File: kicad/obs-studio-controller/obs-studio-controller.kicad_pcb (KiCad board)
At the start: 2 copper layers, 70 parts, among them J1 PWR_SWITCH, J2 EXT_PWR, J3 LEDS, J4 Conn_Display, J5 Conn_02x08_Odd_Even, Q1 2N7002, Q2 SS8050_C2150, Q3 SS8050_C2150, SW1 RotaryEncoder_Switch, SW2 RotaryEncoder_Switch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

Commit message: Routing complete
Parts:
- removed D1: LED5V, LED_SMD:LED_0603_1608Metric
- removed R3: 1k, Resistor_SMD:R_0402_1005Metric
- added J6: GPIO, Connector_PinSocket_2.54mm:PinSocket_1x06_P2.54mm_Vertical, F.Cu at (80.0, 44.0)
- added J7: WS2812, Connector_PinSocket_2.54mm:PinSocket_1x03_P2.54mm_Vertical, F.Cu at (97.5, 19.4)
- J4: footprint Connector_PinHeader_2.54mm:PinHeader_1x08_P2.54mm_Vertical -> custom:DISPLAY
- J5: value Conn_02x08_Odd_Even -> BUTTONS
- moved C9 185.6 mm to (15.5, 19.5), turned to 90 degrees
- moved U5 182.9 mm to (36.5, -26.1), turned to 90 degrees
- moved C10 178.3 mm to (16.9, 19.5), turned to -90 degrees
- moved R12 172.4 mm to (0.00, -17.0), turned to -90 degrees
- moved R19 172.2 mm to (60.0, -17.0), turned to -90 degrees
- moved R10 166.5 mm to (0.00, 3.15), turned to 90 degrees
- moved R11 154.6 mm to (5.00, 3.15), turned to -90 degrees
- moved SW1 154.6 mm to (0.00, 0.00), turned to 90 degrees
- moved R13 151.4 mm to (13.0, 34.8), turned to 180 degrees
- moved R18 150.0 mm to (65.0, 3.15), turned to -90 degrees
- moved R17 148.5 mm to (60.0, 3.15), turned to 90 degrees
- moved Q1 145.9 mm to (16.5, 35.7)
- moved SW3 145.2 mm to (60.0, 0.00), turned to 90 degrees
- moved R20 142.7 mm to (90.0, 3.15), turned to 90 degrees
- moved R22 139.0 mm to (90.0, -17.0), turned to -90 degrees
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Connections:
- C10 pad 2: /Flasher/3V3 -> +3V3
- C3 pad 2: /Flasher/5V -> /AMS1117-5V-3v3/5V
- C4 pad 2: /Flasher/3V3 -> +3V3
- C7 pad 2: /Flasher/5V -> /AMS1117-5V-3v3/5V
- C8 pad 2: /Flasher/5V -> /AMS1117-5V-3v3/5V
- C9 pad 1: /Flasher/3V3 -> +3V3
- J1 pad 1: /+5V -> /AMS1117-5V-3v3/5V
- J1 pad 2: /Flasher/5V -> /VEXT
- J2 pad 3: /Flasher/5V -> /VEXT
- J4 pad 2: +3.3V -> +3V3
- J4 pad 5: +3.3V -> +3V3
- J5 pad 10: /BTN_IN2 -> /BTN_IN3
- J5 pad 12: /BTN_IN2 -> /BTN_IN3
- J5 pad 14: /BTN_IN2 -> /BTN_IN4
- J5 pad 16: /BTN_IN2 -> /BTN_IN4
- J5 pad 6: /BTN_IN1 -> /BTN_IN2
- J5 pad 8: /BTN_IN1 -> /BTN_IN2
- JP1 pad 1: /Flasher/5V -> /VEXT
- JP1 pad 2: /+5V -> /AMS1117-5V-3v3/5V
- R27 pad 2: /Flasher/3V3 -> +3V3
- R28 pad 2: /Flasher/3V3 -> +3V3
- R29 pad 1: /Flasher/3V3 -> +3V3
- R30 pad 1: /Flasher/3V3 -> +3V3
- R31 pad 1: /Flasher/3V3 -> +3V3
- R32 pad 1: /Flasher/5V -> /AMS1117-5V-3v3/5V
- U1 pad 11: unconnected-(U1-Pad11) -> /IO26
- U1 pad 12: unconnected-(U1-Pad12) -> /IO27
- U1 pad 27: unconnected-(U1-Pad27) -> /BTN_IN3
- U1 pad 28: unconnected-(U1-Pad28) -> /BTN_IN4
- U1 pad 29: unconnected-(U1-Pad29) -> /IO5
- U1 pad 6: unconnected-(U1-Pad6) -> /IO34
- U1 pad 7: unconnected-(U1-Pad7) -> /EXT_SENSE
- U1 pad 8: unconnected-(U1-Pad8) -> /IO32
- U1 pad 9: unconnected-(U1-Pad9) -> /IO33
- U4 pad 15: /Flasher/3V3 -> +3V3
- U4 pad 16: /Flasher/5V -> /AMS1117-5V-3v3/5V
- U4 pad 7: /Flasher/5V -> /AMS1117-5V-3v3/5V
- U5 pad 2: /Flasher/3V3 -> +3V3
- U5 pad 3: /Flasher/5V -> /AMS1117-5V-3v3/5V
- USBC1 pad A4-B9: /Flasher/5V -> /AMS1117-5V-3v3/5V
- USBC1 pad B4-A9: /Flasher/5V -> /AMS1117-5V-3v3/5V
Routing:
- net +3V3: track 0.00 -> 291.8 mm, vias 0 -> 27
- net /AMS1117-5V-3v3/5V: track 0.00 -> 153.5 mm, vias 0 -> 1
- net /Flasher/ESP_TX: track 0.00 -> 124.3 mm, vias 0 -> 4
- net /BUTTON_4: track 0.00 -> 122.1 mm, vias 0 -> 1
- net /Flasher/ESP_RX: track 0.00 -> 120.6 mm, vias 0 -> 2
- net /IO5: track 0.00 -> 104.6 mm, vias 0 -> 2
- net /EXT_MONITOR: track 0.00 -> 101.2 mm, vias 0 -> 4
- net /Flasher/ESP_EN: track 0.00 -> 91.4 mm, vias 0 -> 2
- net Net-(J3-Pad1): track 0.00 -> 90.1 mm
- net /Flasher/ESP_IO0: track 0.00 -> 85.0 mm, vias 0 -> 4
- net /BUTTON_3: track 0.00 -> 83.9 mm
- net Net-(J3-Pad3): track 0.00 -> 83.3 mm, vias 0 -> 2
- net /BTN_OUT: track 0.00 -> 79.4 mm, vias 0 -> 5
- net Net-(J3-Pad5): track 0.00 -> 78.2 mm, vias 0 -> 2
- net /BUTTON_2: track 0.00 -> 58.9 mm
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- added copper zone on B.Cu, net +3V3
- added copper zone on B.Cu, net GND
- added copper zone on F.Cu, net GND
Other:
- board outline added: 111 x 113.8 mm
- board text added: "+5V"
- board text added: "3V3"
- board text added: "IO16 IO17 IO34 IO33 IO32 IO27 IO26 IO5"
- board text added: "LEDS"
- board text added: "RX"
- board text added: "TX"
- board text added: "WS2812"

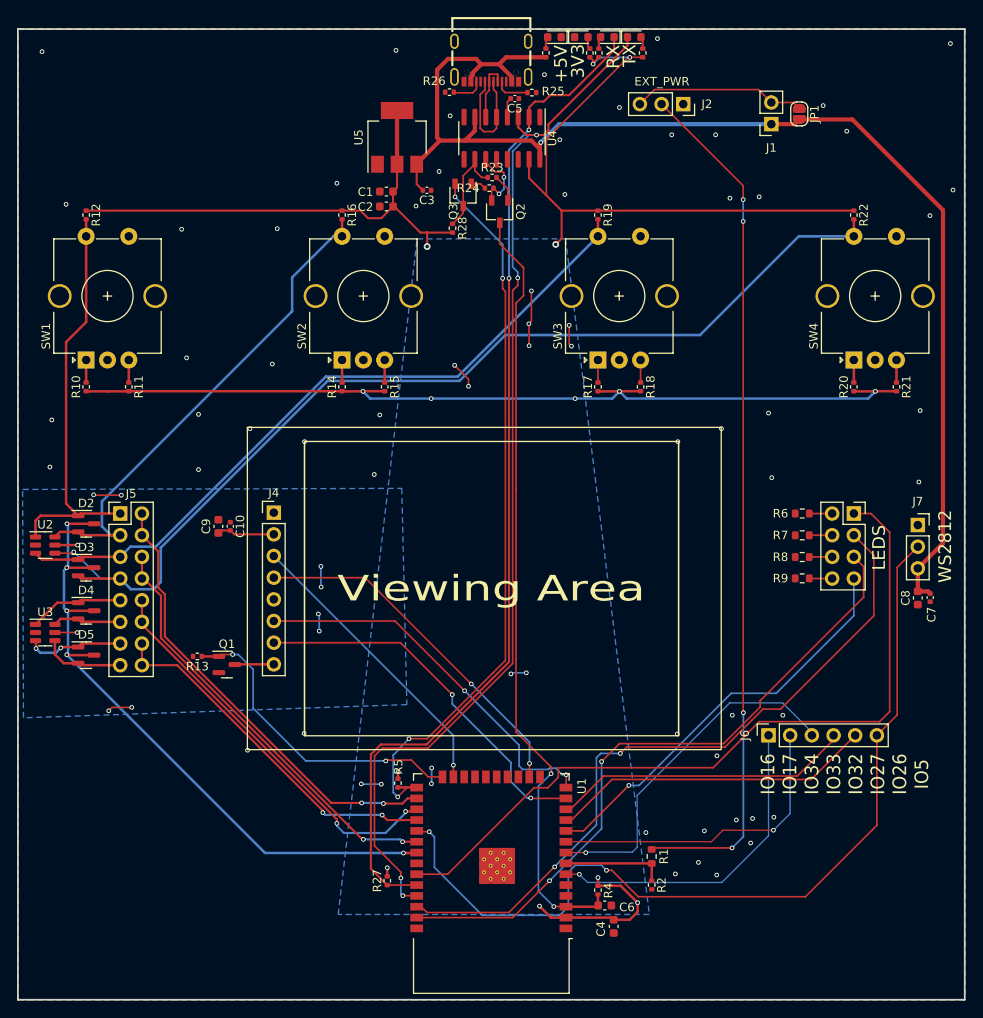
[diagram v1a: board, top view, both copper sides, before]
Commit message: Fixed label, changed edge cuts, added screw holes
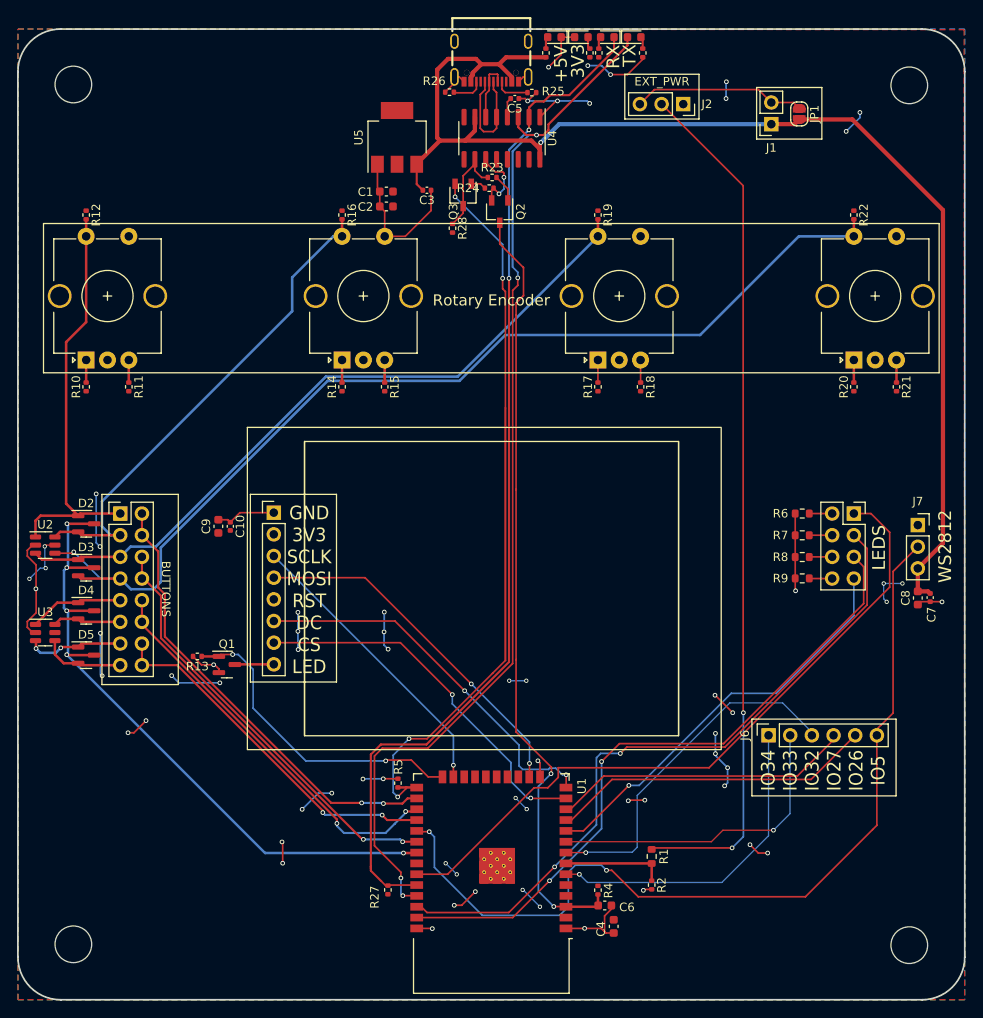
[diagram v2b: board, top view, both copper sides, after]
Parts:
- added REF**: MountingHole_4.3mm_M4, MountingHole:MountingHole_4.3mm_M4, F.Cu at (-1.50, 68.5)
- added REF**: MountingHole_4.3mm_M4, MountingHole:MountingHole_4.3mm_M4, F.Cu at (-1.50, -32.3)
- added REF**: MountingHole_4.3mm_M4, MountingHole:MountingHole_4.3mm_M4, F.Cu at (96.5, 68.6)
- added REF**: MountingHole_4.3mm_M4, MountingHole:MountingHole_4.3mm_M4, F.Cu at (96.5, -32.2)
- moved R27 1.08 mm to (35.4, 62.1), turned to -90 degrees
- renumbered SW4 to SWe
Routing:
- net +3V3: track 291.8 -> 74.3 mm, vias 27 -> 40
- net GND: track 10.5 -> 106.9 mm, vias 64 -> 24
- net Net-(J3-Pad1): track 90.1 -> 81.6 mm
- net Net-(J3-Pad3): track 83.3 -> 81.5 mm
- net /Flasher/ESP_RX: track 120.6 -> 121.2 mm
- net /EXT_MONITOR: vias 4 -> 2
- added copper zone on F.Cu, net +3V3
- removed copper zone on B.Cu, net +3V3
- removed copper zone on F.Cu, net GND
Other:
- outline, holes or cut-outs redrawn
- board text added: "BUTTONS"
- board text added: "GND 3V3 SCLK MOSI RST DC CS LED"
- board text added: "GND OUT +5V"
- board text added: "IO34 IO33 IO32 IO27 IO26 IO5"
- board text added: "Rotary Encoder"
- board text removed: "IO16 IO17 IO34 IO33 IO32 IO27 IO26 IO5"

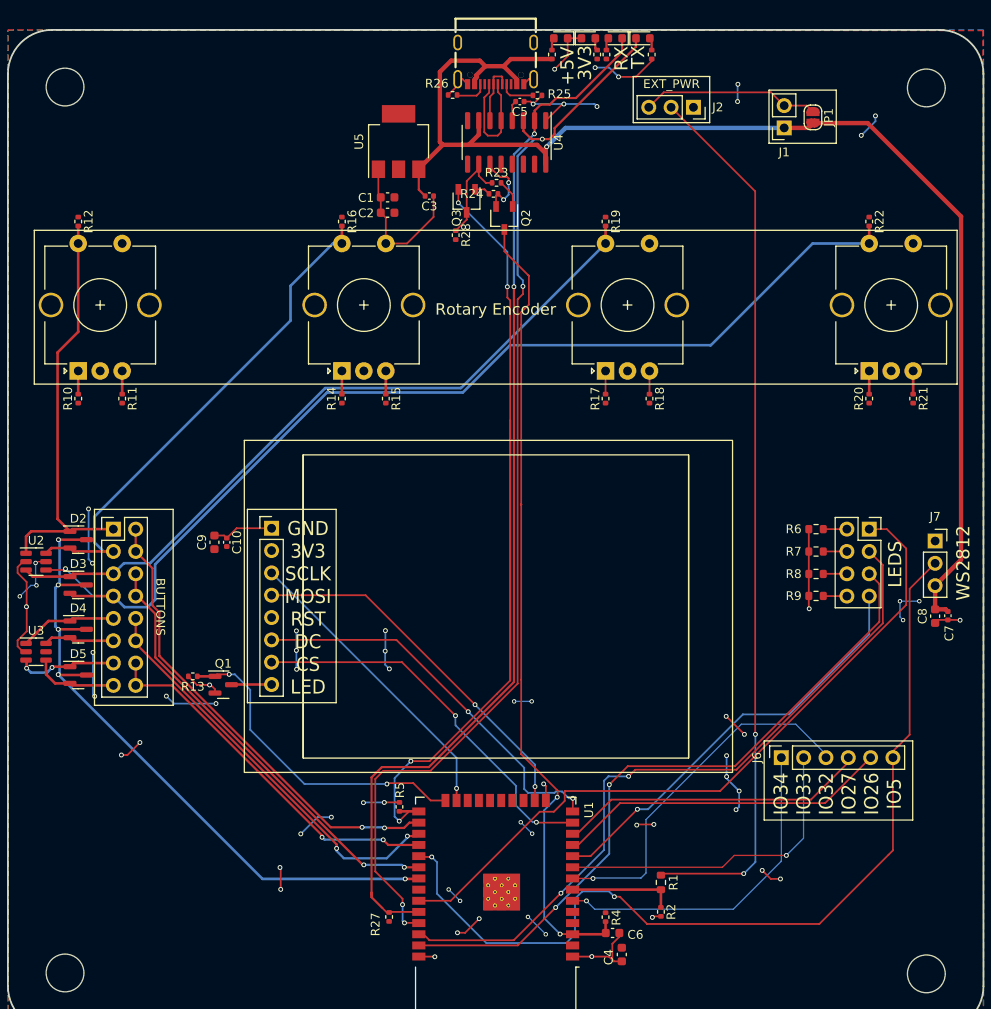
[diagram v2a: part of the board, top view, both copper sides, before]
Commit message: Added some labels
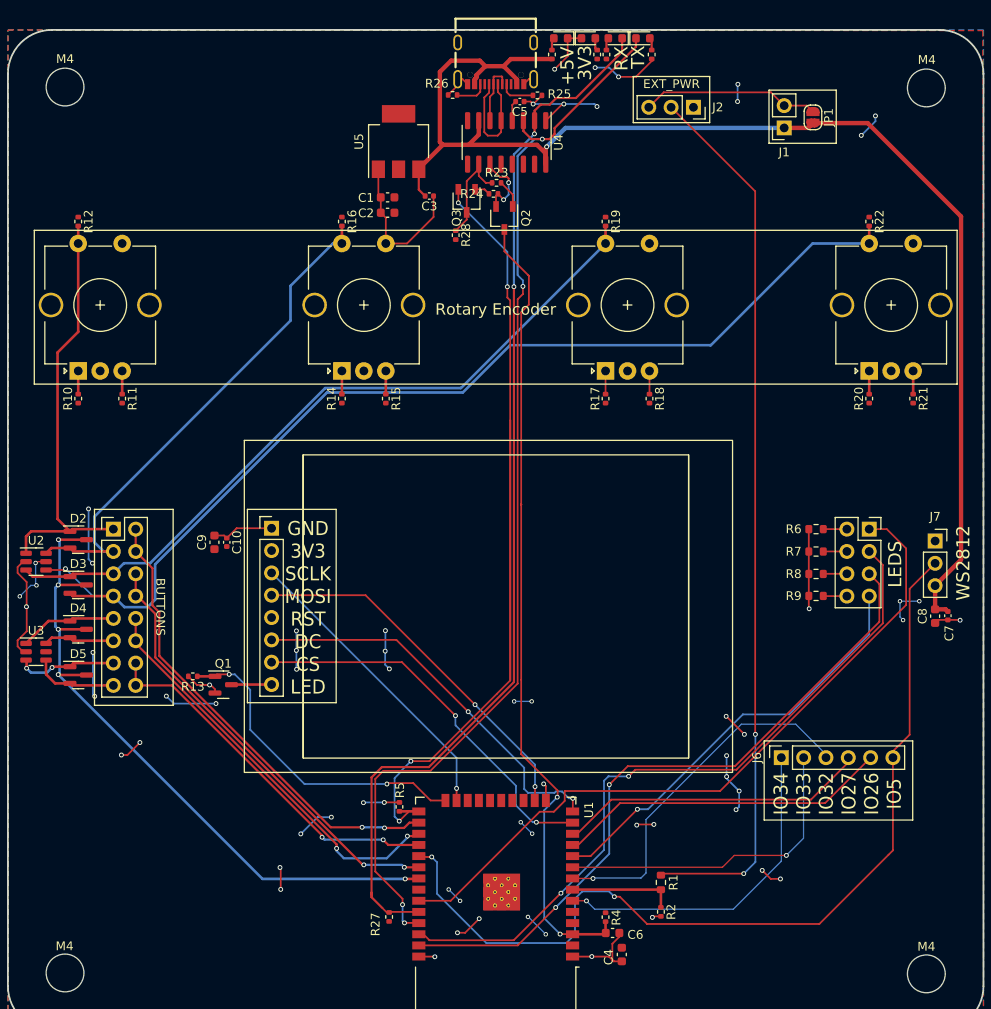
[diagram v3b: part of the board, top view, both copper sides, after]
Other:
- board text added: "M4"
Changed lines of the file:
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@@
     (effects (font (size 1.6 1.5) (thickness 0.3)))
+  )
+  (gr_text "M4" (at -1.5 -35.5) (layer "F.SilkS")
+    (effects (font (size 1 1) (thickness 0.15)))
   )
   (gr_text "Rotary Encoder" (at 47.5 -7) (layer "F.SilkS")
@@
     (effects (font (size 1.5 1.5) (thickness 0.3)))
   )
+  (gr_text "M4" (at 96.5 65.5) (layer "F.SilkS")
+    (effects (font (size 1 1) (thickness 0.15)))
+  )
   (gr_text "LEDS" (at 92.95 22 90) (layer "F.SilkS")
     (effects (font (size 1.5 1.5) (thickness 0.3)))
@@
   (gr_text "+5V" (at 55.65 -34.7 90) (layer "F.SilkS")
     (effects (font (size 1.5 1.5) (thickness 0.3)))
+  )
+  (gr_text "M4" (at -1.55 65.45) (layer "F.SilkS")
+    (effects (font (size 1 1) (thickness 0.15)))
   )
   (gr_text "WS2812" (at 100.7 21.85 90) (layer "F.SilkS")
@@
     (effects (font (size 1 1) (thickness 0.15)))
   )
+  (gr_text "M4" (at 96.55 -35.4) (layer "F.SilkS")
+    (effects (font (size 1 1) (thickness 0.15)))
+  )

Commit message: Updated production files
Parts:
- removed REF** (x4): MountingHole_4.3mm_M4, MountingHole:MountingHole_4.3mm_M4
- removed SWe: RotaryEncoder_Switch, Rotary_Encoder:RotaryEncoder_Alps_EC12E-Switch_Vertical_H20mm_CircularMountingHoles
- added SW4: RotaryEncoder_Switch, Rotary_Encoder:RotaryEncoder_Alps_EC12E-Switch_Vertical_H20mm_CircularMountingHoles, F.Cu at (90.0, 0.00)
- C2: footprint Capacitor_SMD:C_0603_1608Metric -> Capacitor_SMD:C_0402_1005Metric
- moved C1 0.35 mm to (34.9, -19.7)
- moved C2 0.32 mm to (34.9, -18.2)
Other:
- outline, holes or cut-outs redrawn

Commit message: Added rotary 3d model, discovered that the lcsc part number is wrong
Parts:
- SW1, SW2, SW3, SW4: footprint Rotary_Encoder:RotaryEncoder_Alps_EC12E-Switch_Vertical_H20mm_CircularMountingHoles -> custom:RotaryEncoder_Alps_EC12E-Switch_Vertical_H20mm_CircularMountingHoles

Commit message: Fixed rotary encoder
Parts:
- SW1, SW2, SW3, SW4: footprint custom:RotaryEncoder_Alps_EC12E-Switch_Vertical_H20mm_CircularMountingHoles -> custom:SW-TH_EC11K1524406
- moved SW1 7.67 mm to (2.50, -7.25), turned to 0 degrees
- moved SW2 7.67 mm to (32.5, -7.25), turned to 0 degrees
- moved SW3 7.67 mm to (62.5, -7.25), turned to 0 degrees
- moved SW4 7.67 mm to (92.5, -7.25), turned to 0 degrees
- moved R12 5.00 mm to (5.00, -17.0)
- moved R16 5.00 mm to (35.0, -17.0)
- moved R19 5.00 mm to (65.0, -17.0)
- moved R22 5.00 mm to (95.0, -17.0)
- moved C2 1.89 mm to (33.3, -17.2)
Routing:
- net /BUTTON_3: track 83.9 -> 88.9 mm
- net /BUTTON_4: track 122.1 -> 127.1 mm
- net /BUTTON_2: track 58.9 -> 63.3 mm
- net /BUTTON_1: track 48.5 -> 50.6 mm
- net +3V3: track 74.1 -> 75.5 mm
- net GND: track 106.9 -> 108.1 mm, vias 24 -> 25
